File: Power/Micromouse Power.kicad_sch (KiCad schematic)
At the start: 45 parts, among them J1 Battery, J2 Conn_02x08_Odd_Even, SW1 SW_SPST, U1 AMS1117-3.3, U2 TP4056, U3 DRV8837, U4 DRV8837

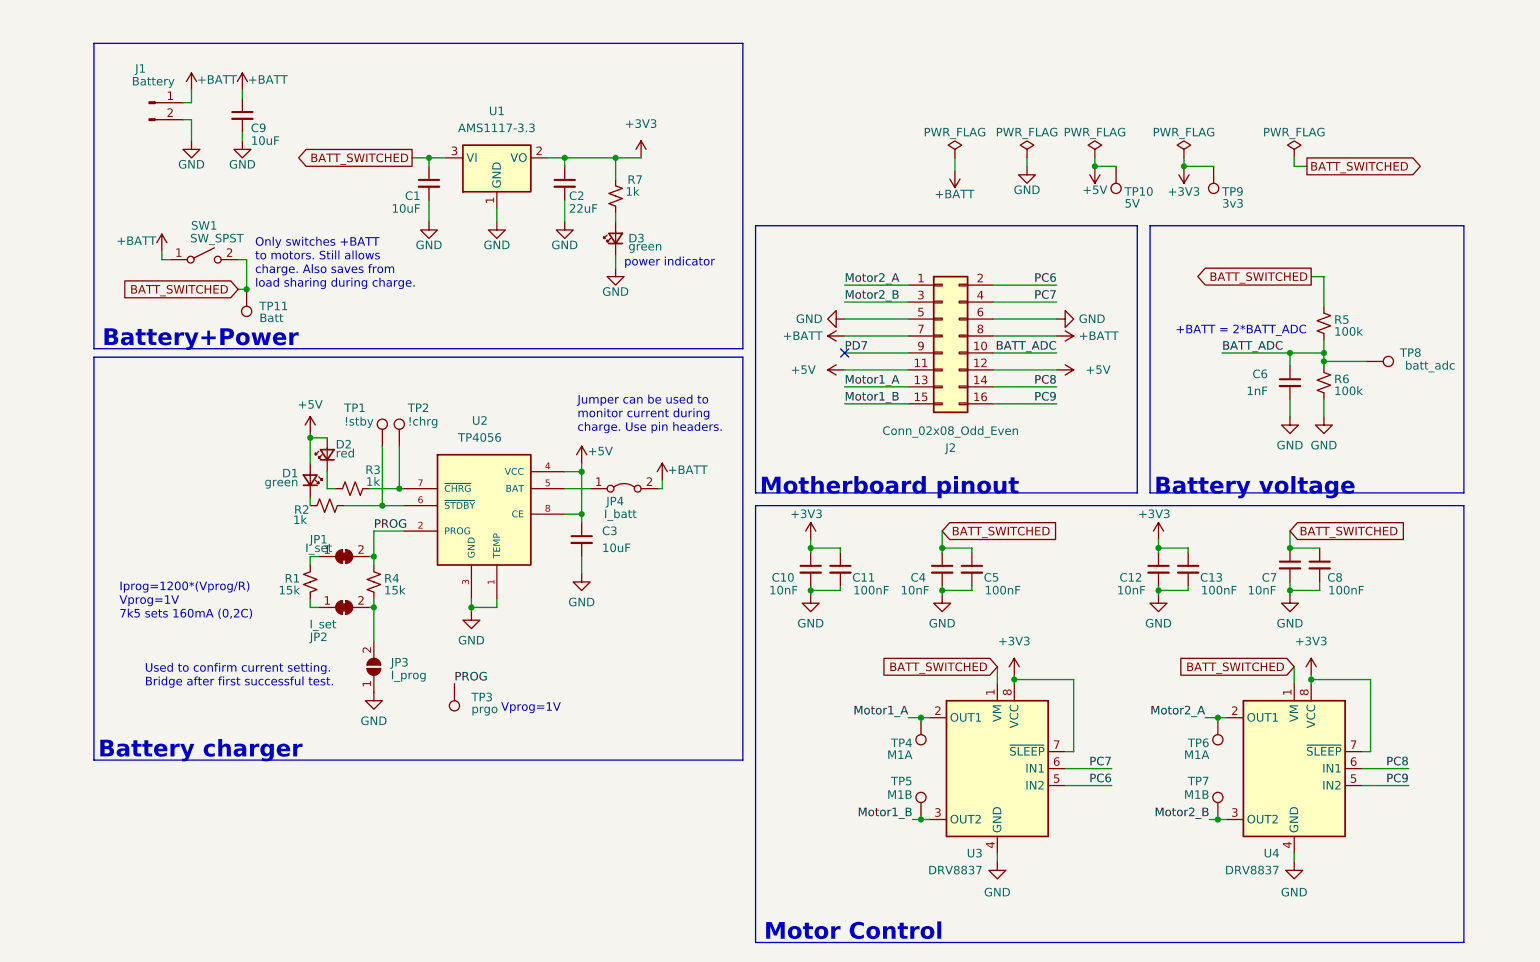
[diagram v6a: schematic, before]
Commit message: Added pmos+switch circuit
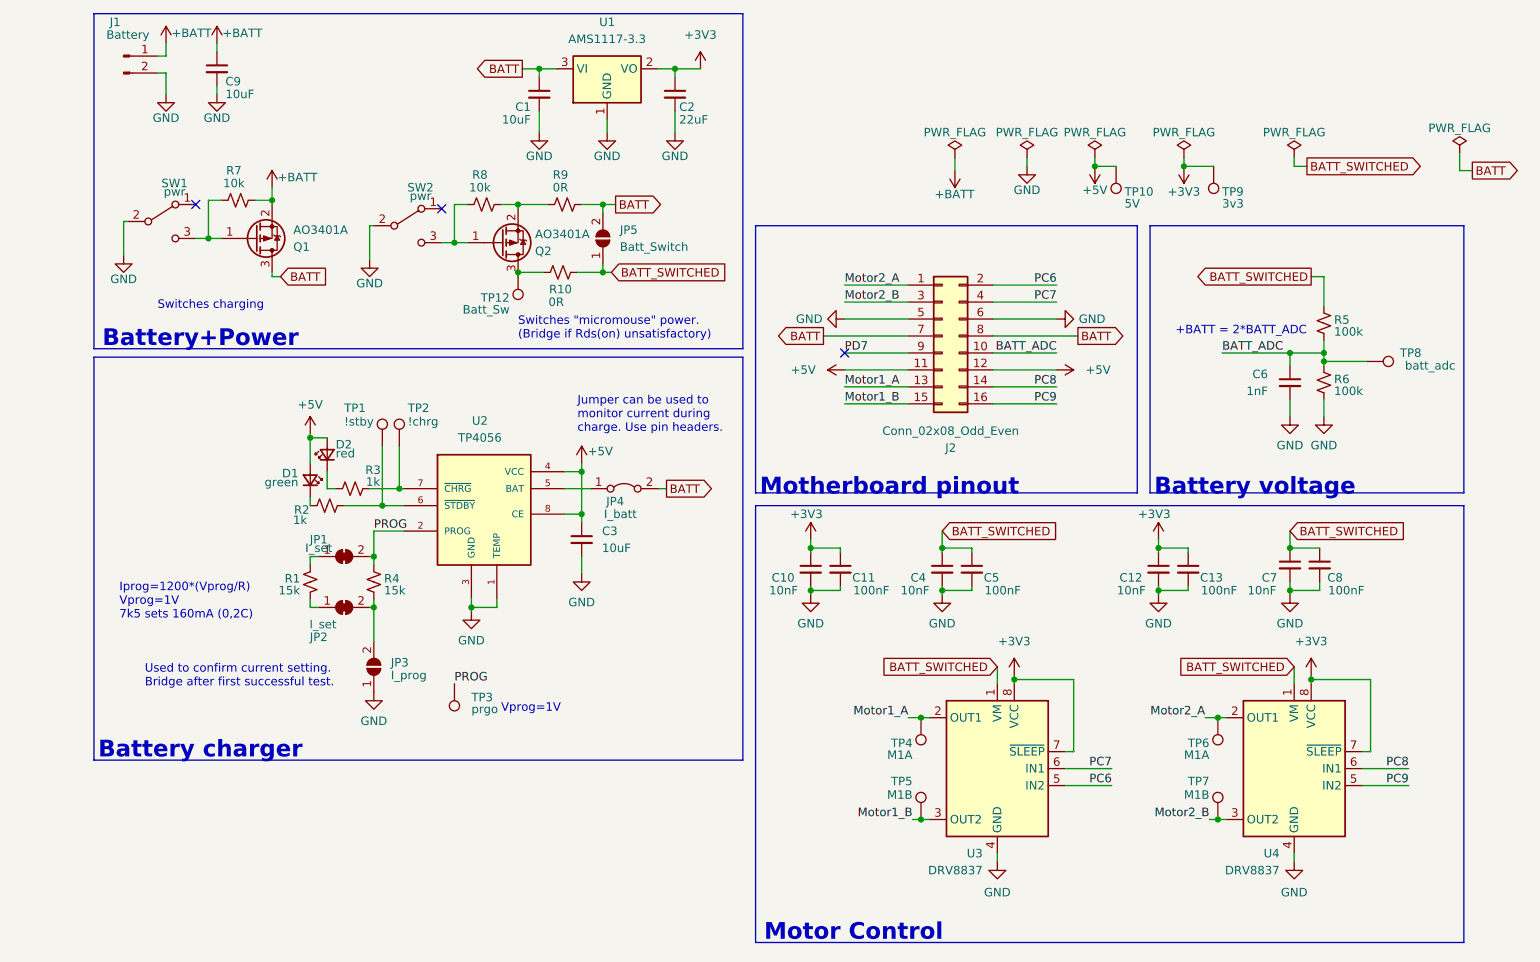
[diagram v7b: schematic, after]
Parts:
- removed D3: green, LED_SMD:LED_0603_1608Metric, symbol Device:LED_Small
- removed TP11: Batt, TestPoint:TestPoint_Pad_D1.0mm, symbol Connector:TestPoint
- added JP5: Batt_Switch, Jumper:SolderJumper-2_P1.3mm_Open_RoundedPad1.0x1.5mm, symbol Jumper:SolderJumper_2_Open
- added Q1, Q2: AO3401A, Package_TO_SOT_SMD:SOT-23, symbol Transistor_FET:AO3401A
- added R10, R9: 0R, Resistor_SMD:R_0603_1608Metric_Pad0.98x0.95mm_HandSolder, symbol Device:R_Small_US
- added R8: 10k, Resistor_SMD:R_0603_1608Metric_Pad0.98x0.95mm_HandSolder, symbol Device:R_Small_US
- added SW2: pwr, Button_Switch_SMD:SW_SPDT_CK-JS102011SAQN, symbol Switch:SW_SPDT
- added TP12: Batt_Sw, TestPoint:TestPoint_Pad_D1.0mm, symbol Connector:TestPoint
- R7: value 1k -> 10k
- SW1: value SW_SPST -> pwr; footprint Button_Switch_SMD:Nidec_Copal_CAS-120A -> Button_Switch_SMD:SW_SPDT_CK-JS102011SAQN; symbol Switch:SW_SPST -> Switch:SW_SPDT; LCSC (none) -> C145857
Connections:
- net +3V3: no longer R7.2
- net +BATT: now also R7.1, Q1.2 (S); no longer J2.7 (Pin_7), J2.8 (Pin_8), JP4.2 (B), SW1.1 (A)
- net BATT_SWITCHED: now also JP5.1 (A), R10.2; no longer C1.1, SW1.2 (B), U1.3 (VI)
- net GND: now also SW1.2 (B), SW2.2 (B)
- new net: Q1.1 (G), R7.2, SW1.3 (C)
- new net: Q2.2 (S), R8.1, R9.2
- new net: Q2.1 (G), R8.2, SW2.3 (C)
- new net: Q2.3 (D), R10.1, TP12.1
- new net BATT: C1.1, J2.7 (Pin_7), J2.8 (Pin_8), JP4.2 (B), JP5.2 (B), Q1.3 (D), R9.1, U1.3 (VI)
- no-connect marks 1 -> 3
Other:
- note added: "Switches "micromouse" power. (Bridge if Rds(on) unsatisfactory)"
- note added: "Switches charging"
- note removed: "Only switches +BATT to motors. Still allows charge. Also saves from load sharing during charge."
- note removed: "power indicator"
- moved on the sheet: C1, C2, C9, J1, R7, U1

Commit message: Assigned footprints, hor. jst and switches
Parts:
- J1: footprint Connector_JST:JST_PH_B2B-PH-K_1x02_P2.00mm_Vertical -> Connector_JST:JST_PH_S2B-PH-K_1x02_P2.00mm_Horizontal
- SW1, SW2: footprint Button_Switch_SMD:SW_SPDT_CK-JS102011SAQN -> MyLibrary:SMD_SPDT
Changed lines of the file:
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@@
       (effects (font (size 1.27 1.27)))
     )
-    (property "Footprint" "Button_Switch_SMD:SW_SPDT_CK-JS102011SAQN" (at 68.58 47.625 0)
+    (property "Footprint" "MyLibrary:SMD_SPDT" (at 68.58 47.625 0)
       (effects (font (size 1.27 1.27)) hide)
     )
@@
       (effects (font (size 1.27 1.27)))
     )
-    (property "Footprint" "Connector_JST:JST_PH_B2B-PH-K_1x02_P2.00mm_Vertical" (at 62.865 22.86 0)
+    (property "Footprint" "Connector_JST:JST_PH_S2B-PH-K_1x02_P2.00mm_Horizontal" (at 62.865 22.86 0)
       (effects (font (size 1.27 1.27)) hide)
     )
@@
       (effects (font (size 1.27 1.27)))
     )
-    (property "Footprint" "Button_Switch_SMD:SW_SPDT_CK-JS102011SAQN" (at 105.41 48.26 0)
-      (effects (font (size 1.27 1.27)) hide)
-    )
+    (property "Footprint" "MyLibrary:SMD_SPDT" (at 105.41 48.26 0)
+      (effects (font (size 1.27 1.27)) hide)
+    )
